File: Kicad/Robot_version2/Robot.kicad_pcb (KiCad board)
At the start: 2 copper layers, 159 x 78.5 mm, 55 parts, among them J1 PositiveBus, J10 LORA, J11 RELAY HEADER, J12 X8R HEADER, J13 SENSOR 1, J14 SENSOR 2, J15 SENSOR 3, J16 SENSOR 4, J2 NegativeBus, J3 PIN HEADER DE0-NANO POWER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

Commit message: rev 2 placement
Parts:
- removed C1, C11: .1uf, Robot:C_Disc_D3.8mm_W2.6mm_P2.50mm
- removed J5: BreakoutHeader, Robot:PinHeader_1x06_P2.54mm_Vertical
- removed JP3: Jumper, Robot:PinHeader_1x02_P2.54mm_Vertical
- removed the MH1 at (21.3, -7.00)
- removed R1, R2: 4.7K, Robot:R_Axial_DIN0204_L3.6mm_D1.6mm_P2.54mm_Vertical
- removed U2: RFM9X, Robot:RFM9X
- added C14: CP1, Robot:CP_Radial_D5.0mm_P2.50mm, F.Cu at (-39.2, 13.9)
- added MH2: MountingHole, Robot:MountingHole_4.3mm_M4, F.Cu at (16.5, -25.5)
- added R8: 4.7K, Robot:R_Axial_DIN0204_L3.6mm_D1.6mm_P2.54mm_Vertical, F.Cu at (-45.6, 16.4)
- added R9: 4.7K, Robot:R_Axial_DIN0204_L3.6mm_D1.6mm_P2.54mm_Vertical, F.Cu at (-43.0, 13.8)
- added U10: LM1085-ADJ, Robot:TO-263-3_TabPin2, F.Cu at (-43.0, 2.92)
- JP1, JP2: moved to B.Cu
- MH1: value MountingHole_4.3mm_M4 -> MountingHole
- MH3: renamed from MH2; value MountingHole_4.3mm_M4 -> MountingHole
- MH4: renamed from MH1; value MountingHole_4.3mm_M4 -> MountingHole
- MH5: renamed from MH3; value MountingHole_4.3mm_M4 -> MountingHole
- MH6: renamed from MH4; value MountingHole_4.3mm_M4 -> MountingHole
- U1: footprint Robot:USB_POWER -> Robot:USB_POWER_flush
- moved U8 66.3 mm to (7.39, -3.22), turned to 90 degrees
- moved J11 56.9 mm to (38.1, -2.94), turned to 270 degrees
- turned JP1 to 270 degrees
- turned JP2 to 90 degrees
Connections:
- C2 pad 1: PWR_8CH_RLY -> PWR_IND_SENSOR
- C5 pad 1: PWR_IND_SENSOR -> PWR_8CH_RLY
- C6 pad 1: PWR_8CH_RLY -> PWR_IND_SENSOR
- C9 pad 1: PWR_IND_SENSOR -> PWR_8CH_RLY
- JP1 pad 2: MISO -> Net-(JP1-Pad2)
- JP1 pad 4: MOSI -> Net-(JP1-Pad4)
- JP1 pad 5: SCK -> Net-(JP1-Pad5)
- JP1 pad 6: CS -> Net-(JP1-Pad6)
- JP1 pad 7: G0 -> Net-(JP1-Pad7)
- JP1 pad 8: RST -> Net-(JP1-Pad8)
- JP1 pad 9: EN -> Net-(JP1-Pad9)
- U1 pad 1: Net-(J2-Pad1) -> Net-(C14-Pad1)
- U1 pad 2: Net-(J1-Pad1) -> GND
- U3 pad 7: PWR_8CH_RLY -> PWR_IND_SENSOR
- U3 pad 8: PWR_8CH_RLY -> PWR_IND_SENSOR
- U6 pad 3: Net-(JP3-Pad2) -> Net-(J1-Pad1)
- U6 pad 4: Net-(JP3-Pad2) -> Net-(J1-Pad1)
- U6 pad 7: PWR_IND_SENSOR -> PWR_8CH_RLY
- U6 pad 8: PWR_IND_SENSOR -> PWR_8CH_RLY
- U8 pad 1: Net-(JP2-Pad17) -> Net-(U8-Pad1)
- U8 pad 2: Net-(JP2-Pad15) -> Net-(U8-Pad2)
- U8 pad 3: Net-(JP2-Pad13) -> Net-(U8-Pad3)
- U8 pad 4: Net-(JP2-Pad9) -> Net-(U8-Pad4)
- U8 pad 5: Net-(JP2-Pad7) -> Net-(U8-Pad5)
- U8 pad 6: Net-(JP2-Pad5) -> Net-(U8-Pad6)
- U8 pad 7: Net-(JP2-Pad2) -> Net-(U8-Pad7)
- U8 pad 8: Net-(JP2-Pad4) -> Net-(U8-Pad8)
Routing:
- net PWR_8CH_RLY: track 140.9 -> 16.1 mm
- net Net-(J1-Pad1): track 212.5 -> 114.5 mm
- net VCC3P3: track 174.3 -> 110.3 mm
- net RST: track 41.1 -> 0.00 mm
- net Net-(JP2-Pad4): track 40.2 -> 0.00 mm
- net Net-(JP2-Pad17): track 38.6 -> 0.00 mm
- net GND: track 495.7 -> 457.6 mm
- net Net-(J2-Pad1): track 202.9 -> 166.6 mm
- net Net-(JP2-Pad15): track 36.0 -> 0.27 mm
- net Net-(JP2-Pad2): track 33.6 -> 0.00 mm
- net Net-(JP2-Pad13): track 32.9 -> 0.00 mm
- net CS: track 31.2 -> 0.00 mm
- net Net-(JP2-Pad9): track 29.1 -> 0.07 mm
- net Net-(JP2-Pad7): track 25.9 -> 0.00 mm
- net Net-(J11-Pad9): track 25.7 -> 0.00 mm
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
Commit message: First draft of rev2
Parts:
- removed J8: Conn_01x05, Robot:PinHeader_1x05_P2.54mm_Vertical
- removed PI1: XT60_CONNECTOR, Robot:XT60PW
- added BT1: Battery_Cell, TerrafirmaComponents:XT60PW, F.Cu at (-47.6, 30.0)
- added BT2: Battery_Cell, TerrafirmaComponents:XT60_M, F.Cu at (-39.0, 34.6)
- moved MH2 28.0 mm to (44.0, -20.7)
- moved J11 0.95 mm to (37.9, -2.02)
- moved U8 0.79 mm to (7.38, -2.43)
- moved C14 0.23 mm to (-39.0, 13.9)
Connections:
- C14 pad 2: GND -> Net-(BT1-Pad1)
- J2 pad 1: Net-(J2-Pad1) -> Net-(BT1-Pad1)
- J2 pad 2: Net-(J2-Pad1) -> Net-(BT1-Pad1)
- J2 pad 3: Net-(J2-Pad1) -> Net-(BT1-Pad1)
- JP1 pad 5: Net-(JP1-Pad5) -> RI8
- JP1 pad 7: Net-(JP1-Pad7) -> RI7
- JP1 pad 9: Net-(JP1-Pad9) -> RI6
- JP2 pad 31: Net-(J8-Pad1) -> RI5
- JP2 pad 33: Net-(J8-Pad2) -> RI4
- JP2 pad 35: Net-(J8-Pad3) -> RI3
- JP2 pad 37: Net-(J8-Pad4) -> RI2
- JP2 pad 39: Net-(J8-Pad5) -> RI1
- R8 pad 2: GND -> Net-(BT1-Pad1)
- U1 pad 2: GND -> Net-(BT1-Pad1)
- U3 pad 1: Net-(J2-Pad1) -> Net-(BT1-Pad1)
- U3 pad 2: Net-(J2-Pad1) -> Net-(BT1-Pad1)
- U4 pad 1: Net-(J2-Pad1) -> Net-(BT1-Pad1)
- U4 pad 2: Net-(J2-Pad1) -> Net-(BT1-Pad1)
- U5 pad 1: Net-(J2-Pad1) -> Net-(BT1-Pad1)
- U5 pad 2: Net-(J2-Pad1) -> Net-(BT1-Pad1)
- U6 pad 1: Net-(J2-Pad1) -> Net-(BT1-Pad1)
- U6 pad 2: Net-(J2-Pad1) -> Net-(BT1-Pad1)
- U8 pad 1: Net-(U8-Pad1) -> RI1
- U8 pad 2: Net-(U8-Pad2) -> RI2
- U8 pad 3: Net-(U8-Pad3) -> RI3
- U8 pad 4: Net-(U8-Pad4) -> RI4
- U8 pad 5: Net-(U8-Pad5) -> RI5
- U8 pad 6: Net-(U8-Pad6) -> RI6
- U8 pad 7: Net-(U8-Pad7) -> RI7
- U8 pad 8: Net-(U8-Pad8) -> RI8
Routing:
- net Net-(BT1-Pad1): track 0.00 -> 259.1 mm
- net Net-(J2-Pad1): track 166.6 -> 0.00 mm
- net Net-(BT1-Pad2): track 114.5 -> 251.1 mm
- net GND: track 457.6 -> 541.9 mm
- net VCC3P3: track 110.3 -> 183.2 mm, vias 0 -> 1
- net Net-(C14-Pad1): track 0.00 -> 70.6 mm
- net RI5: track 0.00 -> 60.8 mm, vias 0 -> 2
- net RI4: track 0.00 -> 59.7 mm, vias 0 -> 2
- net RI3: track 0.00 -> 58.5 mm, vias 0 -> 2
- net RI2: track 0.00 -> 57.4 mm, vias 0 -> 2
- net RI1: track 0.00 -> 55.8 mm, vias 0 -> 2
- net Net-(J11-Pad2): track 0.00 -> 51.1 mm, vias 0 -> 2
- net Net-(J11-Pad3): track 0.00 -> 45.5 mm
- net Net-(J11-Pad4): track 0.00 -> 40.6 mm
- net Net-(J11-Pad5): track 0.00 -> 35.8 mm
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
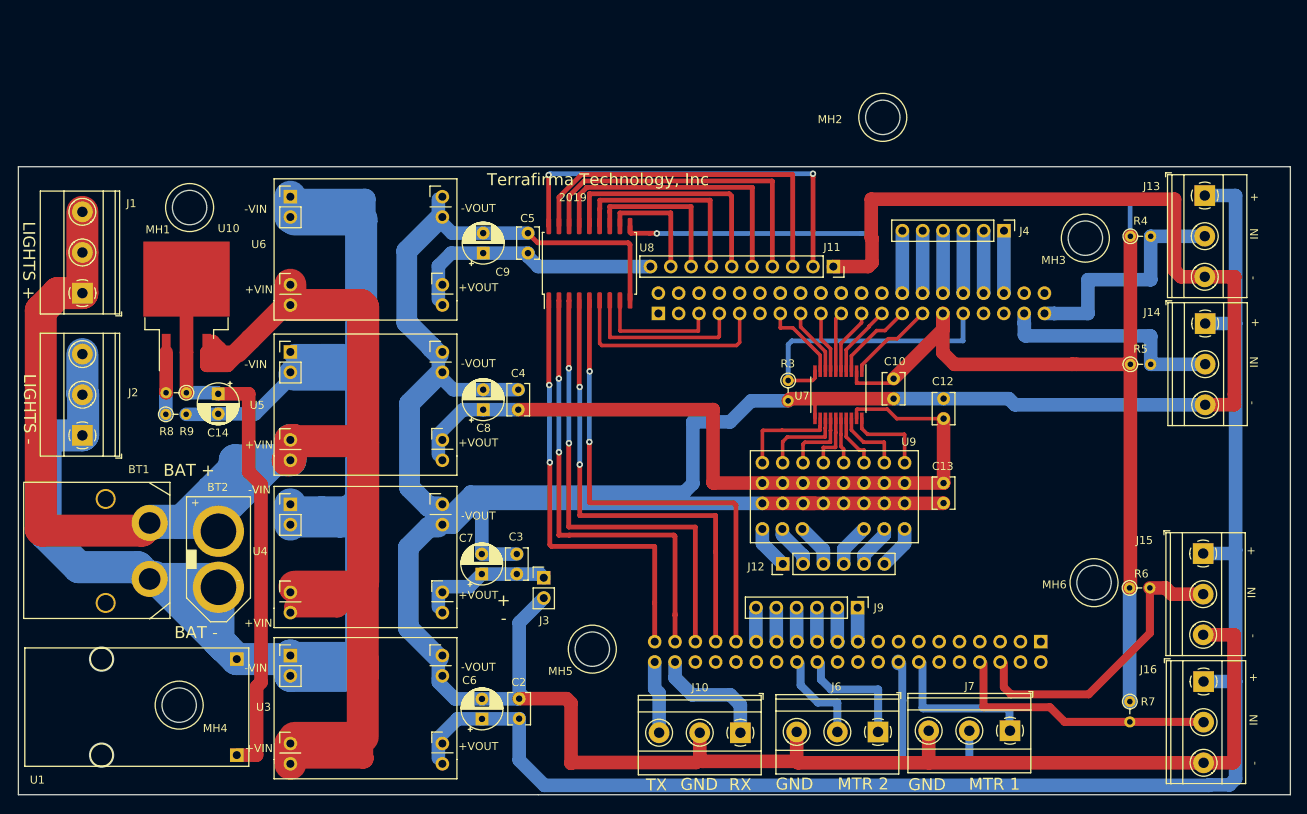
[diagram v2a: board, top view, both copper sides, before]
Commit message: fixed usb
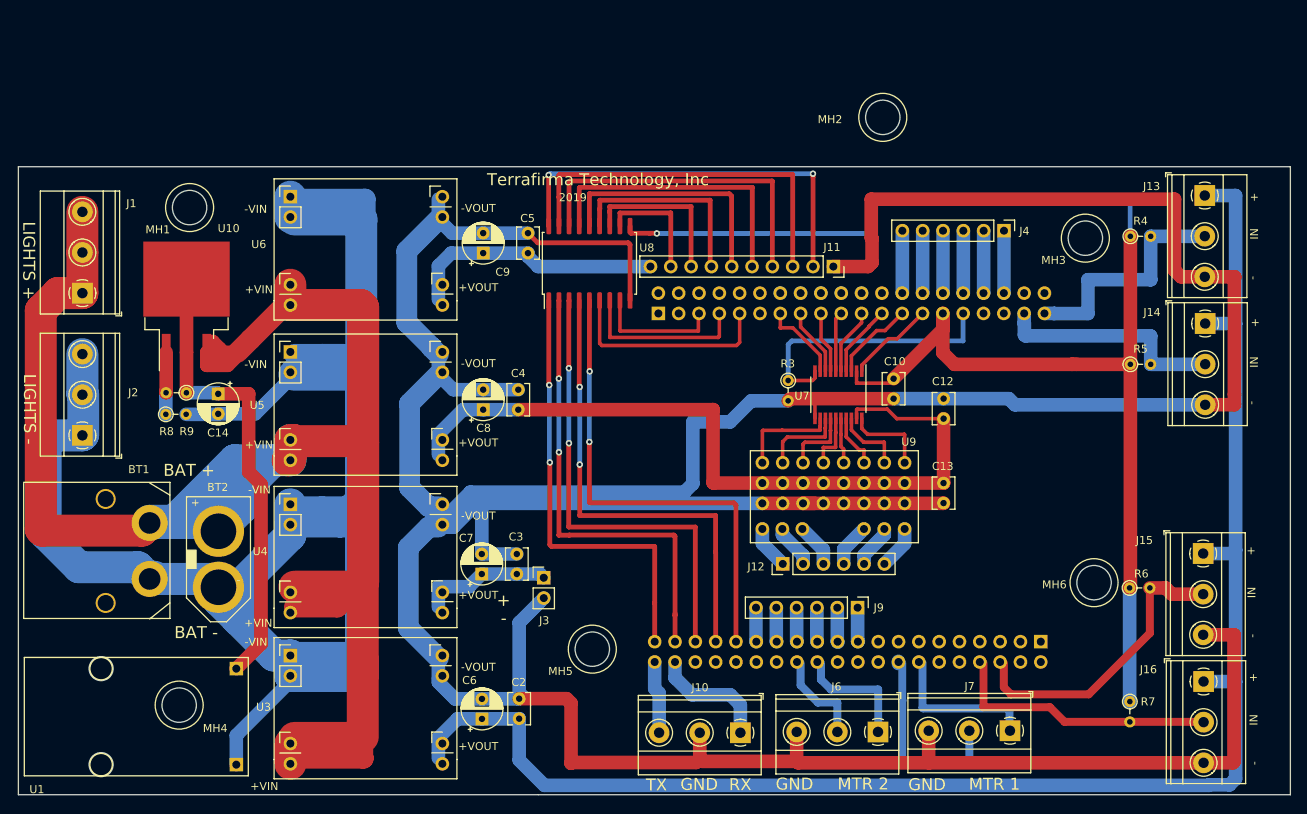
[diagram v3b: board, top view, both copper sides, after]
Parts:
- moved U1 1.19 mm to (-36.8, 60.2)
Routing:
- net Net-(BT1-Pad2): track 251.1 -> 271.5 mm
- net Net-(BT1-Pad1): track 259.1 -> 279.1 mm
- net Net-(C14-Pad1): track 70.6 -> 58.3 mm
- net Net-(J11-Pad3): track 45.5 -> 47.1 mm
- net Net-(J11-Pad4): track 40.6 -> 41.7 mm
- net Net-(J11-Pad5): track 35.8 -> 36.3 mm

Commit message: moved parts closer
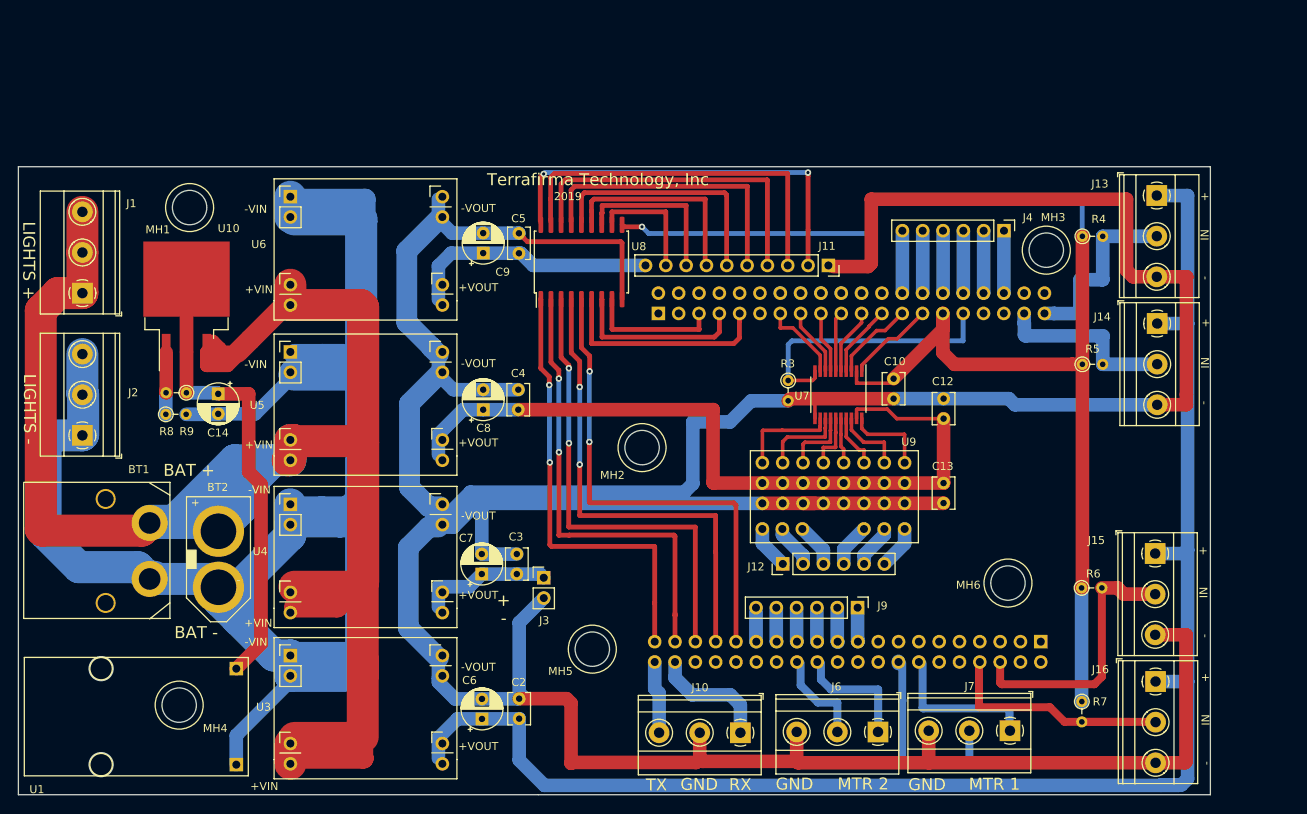
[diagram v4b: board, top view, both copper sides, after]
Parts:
- moved MH2 51.1 mm to (14.0, 20.6)
- moved MH6 10.8 mm to (59.7, 37.5)
- moved J13 6.00 mm to (78.3, -10.9)
- moved J14 6.00 mm to (78.3, 5.10)
- moved J15 6.00 mm to (78.1, 33.9)
- moved J16 6.00 mm to (78.2, 49.9)
- moved R4 6.00 mm to (69.0, -5.80)
- moved R5 6.00 mm to (69.0, 10.2)
- moved R6 6.00 mm to (68.9, 38.1)
- moved R7 6.00 mm to (68.9, 52.4)
- moved MH3 5.11 mm to (64.5, -4.07)
- moved C5 1.13 mm to (-1.43, -3.68)
- moved U8 1.01 mm to (6.38, -2.59)
- moved J11 0.64 mm to (37.2, -2.16)
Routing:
- net GND: track 541.9 -> 523.6 mm
- net VCC3P3: track 183.2 -> 165.0 mm
- net SENSOR2: track 28.9 -> 22.9 mm
- net SENSOR1: track 29.7 -> 23.9 mm
- net PWR_IND_SENSOR: track 198.8 -> 195.1 mm
- net SENSOR3: track 37.5 -> 33.9 mm
- net PWR_8CH_RLY: track 32.3 -> 31.4 mm
- net RI1: track 55.8 -> 56.5 mm
- net RI4: track 59.7 -> 60.3 mm
- net RI5: track 60.8 -> 61.4 mm
- net RI2: track 57.4 -> 58.0 mm
- net RI3: track 58.5 -> 59.0 mm
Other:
- board size 159 x 78.5 mm -> 149 x 78.5 mm
